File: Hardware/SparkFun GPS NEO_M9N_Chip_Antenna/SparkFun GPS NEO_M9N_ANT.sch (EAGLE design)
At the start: 48 parts, among them J2 Qwiic Right Angle, J4 Qwiic Right Angle, U1 U-BLOX_NEO-M9N, U2 3.3V, Y1 GPS_CHIP_ANTENNAW3011

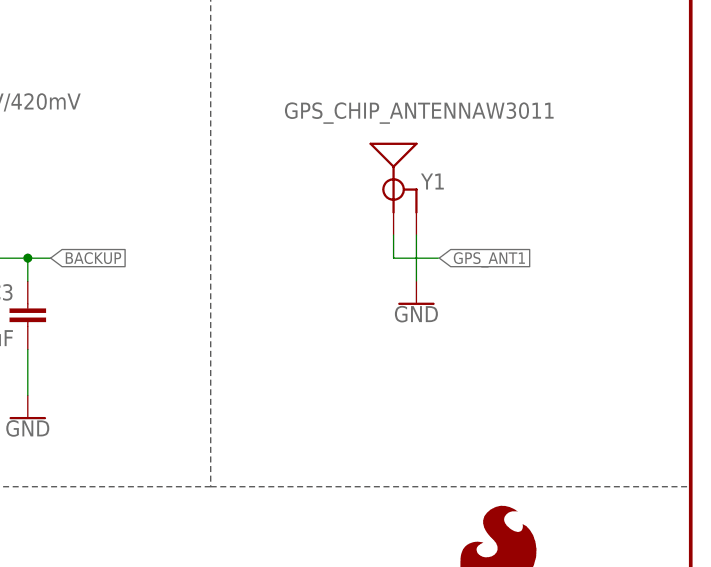
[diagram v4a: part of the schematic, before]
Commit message: Moves left qwiic connector down to match right one, updates measures, moves some vias
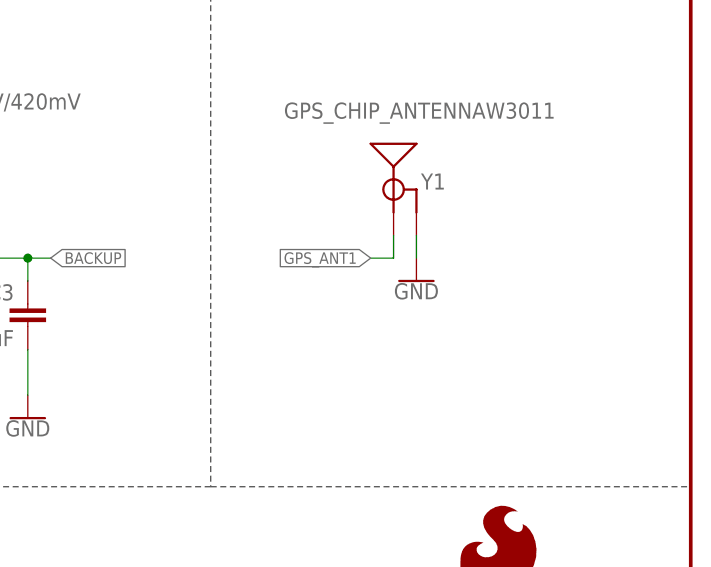
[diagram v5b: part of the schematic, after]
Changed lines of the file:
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@@
 <attribute name="VALUE" x="129.54" y="127" size="1.778" layer="96" font="vector"/>
 </instance>
-<instance part="GND27" gate="1" x="218.44" y="81.28" smashed="yes">
-<attribute name="VALUE" x="218.44" y="81.026" size="1.778" layer="96" font="vector" align="top-center"/>
+<instance part="GND27" gate="1" x="218.44" y="83.82" smashed="yes">
+<attribute name="VALUE" x="218.44" y="83.566" size="1.778" layer="96" font="vector" align="top-center"/>
 </instance>
 <instance part="C4" gate="G$1" x="228.6" y="154.94" smashed="yes">
@@
 <segment>
 <pinref part="Y1" gate="G$1" pin="GND"/>
-<wire x1="218.44" y1="88.9" x2="218.44" y2="83.82" width="0.1524" layer="91"/>
+<wire x1="218.44" y1="88.9" x2="218.44" y2="86.36" width="0.1524" layer="91"/>
 <pinref part="GND27" gate="1" pin="GND"/>
 </segment>
@@
 <net name="GPS_ANT1" class="3">
 <segment>
-<label x="220.98" y="86.36" size="1.27" layer="95" xref="yes"/>
-<wire x1="215.9" y1="86.36" x2="220.98" y2="86.36" width="0.1524" layer="91"/>
+<label x="213.36" y="86.36" size="1.27" layer="95" rot="R180" xref="yes"/>
+<wire x1="215.9" y1="86.36" x2="213.36" y2="86.36" width="0.1524" layer="91"/>
 <wire x1="215.9" y1="86.36" x2="215.9" y2="88.9" width="0.1524" layer="91"/>
 <pinref part="Y1" gate="G$1" pin="SIGNAL"/>

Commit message: Removes local eagle library and replaces part from that library with part from SparkFun Eagle Library
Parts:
- U1: device gps:U-BLOX_NEO-M9N -> SparkFun-GPS:U-BLOX_NEO-M9N
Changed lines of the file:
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@@
 <part name="SUPPLY11" library="SparkFun-PowerSymbols" deviceset="5V" device=""/>
 <part name="LOGO2" library="SparkFun-Aesthetics" deviceset="SFE_LOGO_NAME_FLAME" device=".1_INCH"/>
-<part name="U1" library="gps" deviceset="U-BLOX_NEO-M9N" device=""/>
+<part name="U1" library="SparkFun-GPS" deviceset="U-BLOX_NEO-M9N" device=""/>
 <part name="PWR\" library="SparkFun-Jumpers" deviceset="JUMPER-SMT_2_NC_TRACE" device="_SILK" package3d_urn="urn:adsk.eagle:package:39281/1" value="JUMPER-SMT_2_NC_TRACE_SILK"/>
 <part name="D3" library="SparkFun-IC-Power" deviceset="PRTR5V0U2" device="F"/>

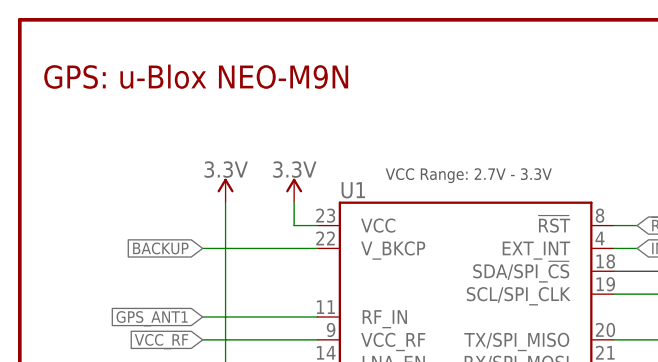
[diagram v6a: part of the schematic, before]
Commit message: Fixes "u-blox" typos in schematic
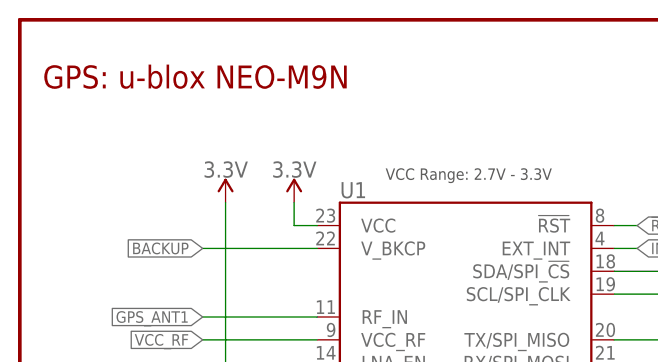
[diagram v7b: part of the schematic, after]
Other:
- note added: "GPS: u-blox NEO-M9N"
- note removed: "GPS: u-Blox NEO-M9N"
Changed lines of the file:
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@@
 <?xml version="1.0" encoding="utf-8"?>
 <!DOCTYPE eagle SYSTEM "eagle.dtd">
-<eagle version="9.5.1">
+<eagle version="9.6.2">
 <drawing>
 <settings>
@@
 <text x="2.54" y="99.06" size="2.54" layer="94" font="vector">LEDs and Jumpers</text>
 <text x="149.86" y="116.84" size="2.54" layer="94" font="vector">Hot Start Battery</text>
-<text x="2.54" y="177.8" size="2.54" layer="94" font="vector">GPS: u-Blox NEO-M9N </text>
+<text x="2.54" y="177.8" size="2.54" layer="94" font="vector">GPS: u-blox NEO-M9N </text>
 <wire x1="73.66" y1="106.68" x2="73.66" y2="0" width="0.1524" layer="97" style="shortdash"/>
 <text x="198.12" y="116.84" size="2.54" layer="94" font="vector">Chip Antenna</text>
